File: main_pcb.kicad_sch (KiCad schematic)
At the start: 93 parts, among them J1 trig, J2 Synth_power_2x5, J3 pitch cv, J4 decay cv, J5 cv_shape, J6 accent, J7 OUT, Q1 2N3904, Q2 2N3904, Q5 2N3904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

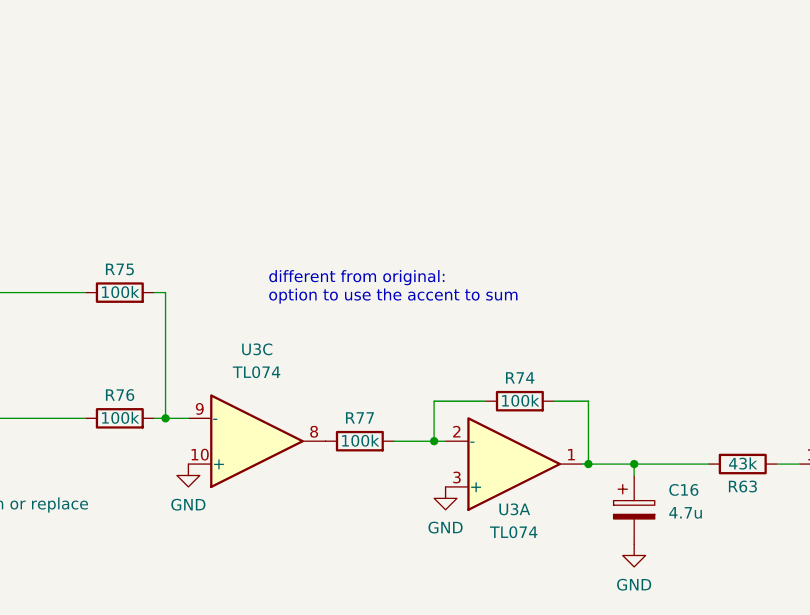
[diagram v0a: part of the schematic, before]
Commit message: fix opampon ctrl pcb, fix accent and make slide pot slot 0.2mm wider
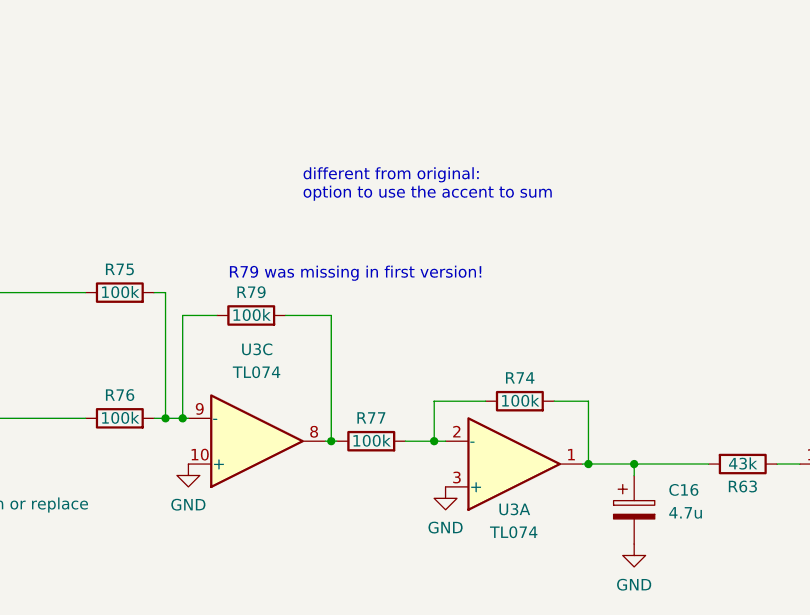
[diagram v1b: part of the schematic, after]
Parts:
- added R79: 100k, ao_tht:R_Axial_DIN0207_L6.3mm_D2.5mm_P10.16mm_Horizontal, symbol ao_symbols:R
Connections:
- net at R75.2, R76.2, U3.9 (-): now also R79.1
- net at R77.1, U3.8: now also R79.2
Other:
- note added: "R79 was missing in first version!"
- moved on the sheet: R77
